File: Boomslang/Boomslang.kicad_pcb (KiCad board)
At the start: 2 copper layers, 100 x 100 mm, 99 parts, among them J1 Screw_Terminal_01x04, J2 Screw_Terminal_01x04, J3 Screw_Terminal_01x04, J4 01x04, J5 Screw_Terminal_01x02, J6 Screw_Terminal_01x02, Q1 IRLZ44N, Q10 2N3904, Q11 IRLZ44N, Q12 2N3904, Q13 2N3904, Q14 2N3904, Q15 2N3906, Q16 2N3904, Q17 IRLZ44N, Q18 2N3904, Q19 2N2222A, Q2 2N3904, Q20 2N2222A, Q3 2N3906, Q4 2N3904, Q5 2N3904, Q6 2N3904, Q7 2N3904, Q8 2N3904, Q9 2N3906, U1 L7805

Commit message: Break out GPIO2 battery sense and GPIO12-14 test points
Adds the GPIO2 12V battery-voltage sense (1:11 divider, matches
firmware's PIN_BATTERY/BATTERY_DIVIDER_RATIO) and breaks out
GPIO12-14 as spare test points for timing tests and similar bring-up
work. Regenerated gerbers and schematic/board renders to match.
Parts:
- added C13: 100 pF, Capacitor_THT:C_Disc_D5.0mm_W2.5mm_P5.00mm, F.Cu at (108.0, 136.7)
- added J7: Conn_01x04_Pin, Connector_PinSocket_2.54mm:PinSocket_1x04_P2.54mm_Vertical, F.Cu at (143.3, 102.6)
- added R45: 100k, Resistor_THT:R_Axial_DIN0207_L6.3mm_D2.5mm_P7.62mm_Horizontal, F.Cu at (127.5, 86.6)
- added R46: 100k, Resistor_THT:R_Axial_DIN0207_L6.3mm_D2.5mm_P7.62mm_Horizontal, F.Cu at (154.4, 51.6)
- added R47: 100k, Resistor_THT:R_Axial_DIN0207_L6.3mm_D2.5mm_P7.62mm_Horizontal, F.Cu at (165.9, 81.8)
- added R48: 100k, Resistor_THT:R_Axial_DIN0207_L6.3mm_D2.5mm_P7.62mm_Horizontal, F.Cu at (168.1, 112.1)
- added R49: 10k, Resistor_THT:R_Axial_DIN0207_L6.3mm_D2.5mm_P7.62mm_Horizontal, F.Cu at (108.0, 134.4)
- added R50: 100k, Resistor_THT:R_Axial_DIN0207_L6.3mm_D2.5mm_P7.62mm_Horizontal, F.Cu at (104.6, 126.7)
- D10, D8, D9: value LED -> WHITE/BLUE LED
- D4, D5, D6, D7: value LED -> RED LED
- R11, R24, R3: value 10k -> 2k2
- moved R34 5.36 mm to (179.6, 113.0)
- moved Q6 5.00 mm to (154.4, 67.1)
- moved R22 3.43 mm to (178.8, 83.3)
- moved D2 1.78 mm to (103.1, 90.4)
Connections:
- DB1 pad 18: unconnected-(DB1-12-Pad18) -> Net-(DB1-12)
- DB1 pad 19: unconnected-(DB1-13-Pad19) -> Net-(DB1-13)
- DB1 pad 20: unconnected-(DB1-14-Pad20) -> Net-(DB1-14)
- DB1 pad 40: unconnected-(DB1-2-Pad40) -> PWRSENSE
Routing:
- net CONTINUITY2: track 15.9 -> 26.4 mm
- net PWRSENSE: track 0.00 -> 10.3 mm
- net CONTINUITY3: track 19.9 -> 28.9 mm
- net Net-(DB1-14): track 0.00 -> 5.59 mm
- net Net-(DB1-13): track 0.00 -> 5.59 mm
- net Net-(DB1-12): track 0.00 -> 5.59 mm
- net Net-(J3-Pin_1): track 24.1 -> 20.5 mm
- net +12V: track 157.0 -> 160.4 mm
- net FAILSAFE: track 156.2 -> 153.5 mm
- net Net-(Q2-B): track 60.6 -> 63.4 mm
- net Net-(Q6-B): track 33.3 -> 35.8 mm
- net SENSEFAILSAFE: track 64.0 -> 66.0 mm
- net FAULT: track 153.8 -> 155.6 mm
- net Net-(J2-Pin_1): track 27.8 -> 26.2 mm
- net SENSE1: track 60.7 -> 61.9 mm
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
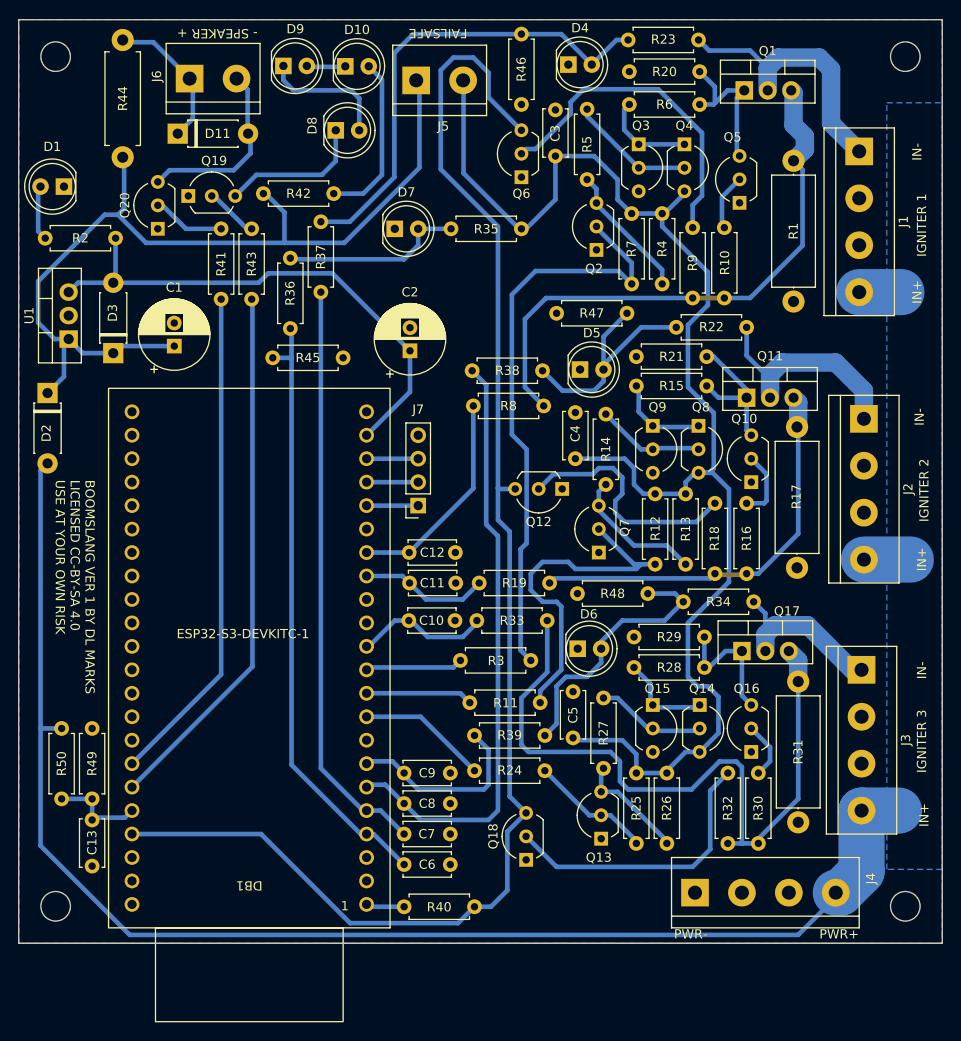
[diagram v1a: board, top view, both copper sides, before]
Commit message: Add snubbers to MOSFET drains
RC snubber on each channel's IRLZ44N drain to damp switching
transients from the igniter/wiring inductance. Regenerated gerbers
and schematic/board renders to match.
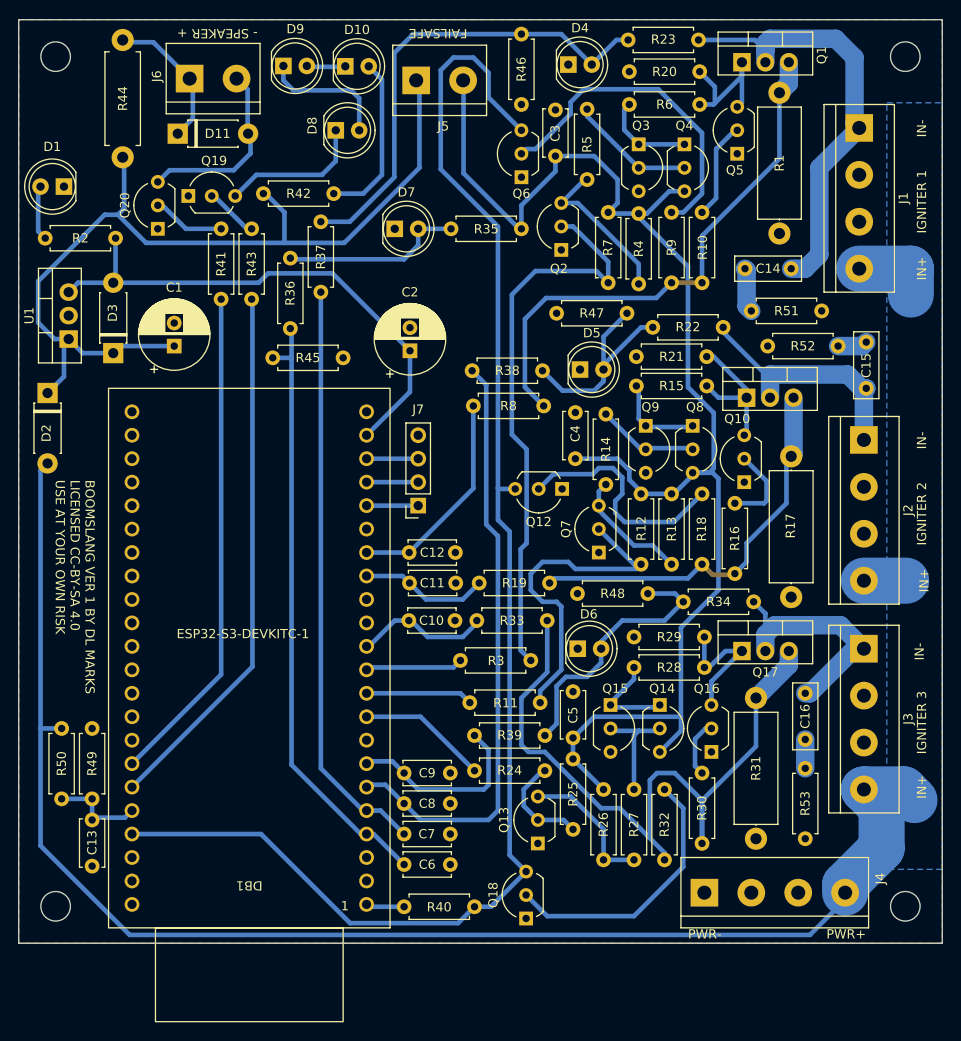
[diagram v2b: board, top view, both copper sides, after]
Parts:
- added C14: 220 nF, Capacitor_THT:C_Rect_L7.0mm_W2.5mm_P5.00mm, F.Cu at (183.6, 77.0)
- added C15: 220 nF, Capacitor_THT:C_Rect_L7.0mm_W2.5mm_P5.00mm, F.Cu at (191.8, 89.9)
- added C16: 220 nF, Capacitor_THT:C_Rect_L7.0mm_W2.5mm_P5.00mm, F.Cu at (185.2, 122.9)
- added R51: 2R2, Resistor_THT:R_Axial_DIN0207_L6.3mm_D2.5mm_P7.62mm_Horizontal, F.Cu at (179.3, 81.5)
- added R52: 2R2, Resistor_THT:R_Axial_DIN0207_L6.3mm_D2.5mm_P7.62mm_Horizontal, F.Cu at (188.7, 85.3)
- added R53: 2R2, Resistor_THT:R_Axial_DIN0207_L6.3mm_D2.5mm_P7.62mm_Horizontal, F.Cu at (185.2, 131.1)
- moved R27 10.4 mm to (166.6, 133.3)
- moved R1 7.52 mm to (182.4, 57.9)
- moved R26 7.08 mm to (163.3, 133.3)
- moved R32 7.08 mm to (169.9, 133.3)
- moved R25 7.03 mm to (160.0, 130.0)
- moved Q13 6.88 mm to (156.2, 139.2)
- moved Q18 6.35 mm to (154.9, 147.3)
- moved R30 6.10 mm to (174.0, 139.2)
- moved Q5 5.32 mm to (177.8, 64.5)
- moved R31 4.91 mm to (179.8, 123.4)
- moved Q15 4.57 mm to (164.1, 124.2)
- moved Q16 4.32 mm to (175.0, 129.3)
- moved Q14 4.32 mm to (169.4, 124.2)
- moved Q2 3.81 mm to (158.8, 74.9)
- moved R17 3.24 mm to (183.6, 97.3)
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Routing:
- net Net-(J1-Pin_1): track 29.2 -> 47.5 mm
- net +12V: track 160.4 -> 170.0 mm
- net Net-(J3-Pin_1): track 20.5 -> 28.1 mm
- net Net-(C14-Pad2): track 0.00 -> 4.85 mm
- net Net-(Q5-B): track 6.12 -> 10.6 mm
- net Net-(C15-Pad2): track 0.00 -> 3.23 mm
- net Net-(C16-Pad2): track 0.00 -> 3.13 mm
- net SENSE1: track 61.9 -> 58.8 mm
- net Net-(Q13-C): track 12.2 -> 15.2 mm
- net Net-(J2-Pin_1): track 26.2 -> 29.0 mm
- net CONTINUITY2: track 26.4 -> 23.9 mm
- net Net-(Q2-C): track 14.7 -> 17.1 mm
- net Net-(Q13-B): track 13.3 -> 11.3 mm
- net Net-(Q18-B): track 31.1 -> 29.4 mm
- net Net-(Q10-B): track 7.52 -> 9.11 mm
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
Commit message: Changed snubber resistor footprint
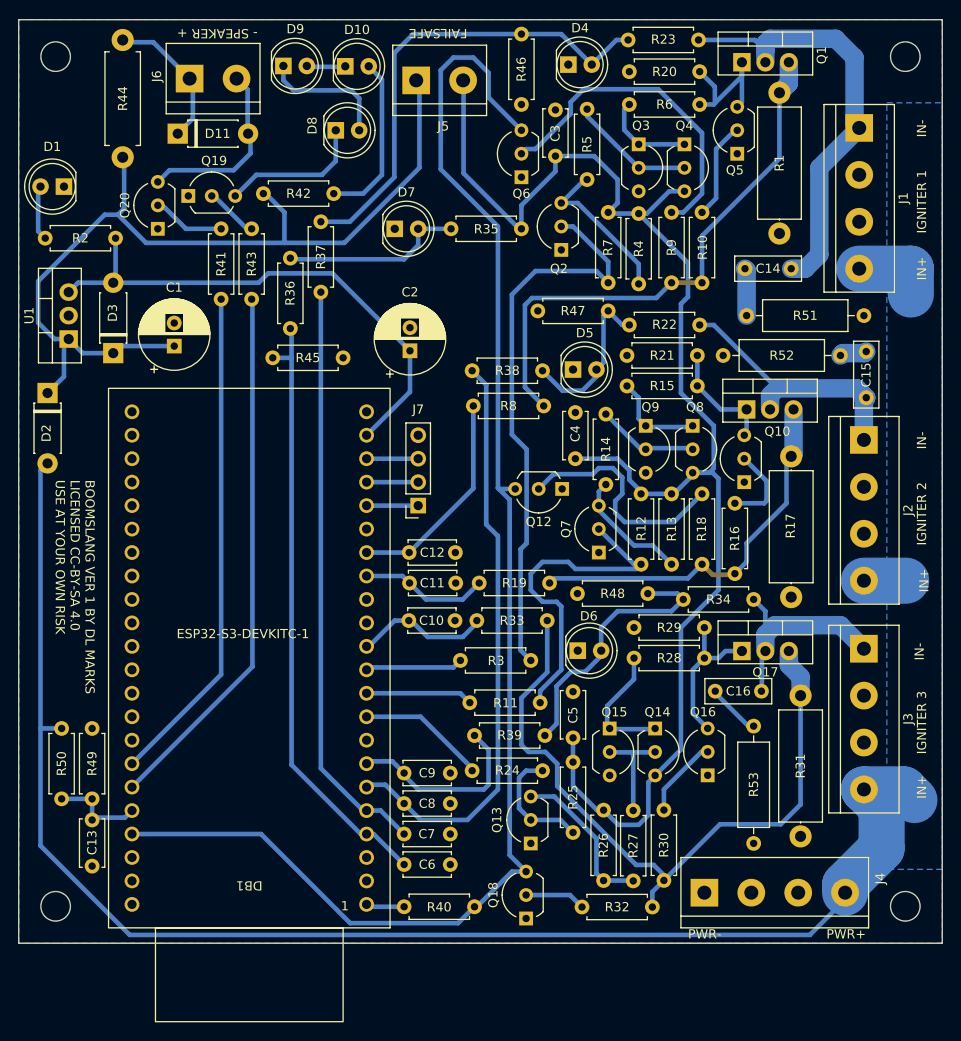
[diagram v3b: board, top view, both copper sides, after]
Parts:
- R51, R52, R53: footprint Resistor_THT:R_Axial_DIN0207_L6.3mm_D2.5mm_P7.62mm_Horizontal -> Resistor_THT:R_Axial_DIN0309_L9.0mm_D3.2mm_P12.70mm_Horizontal
- moved R32 15.6 mm to (161.0, 146.1), turned to 0 degrees
- moved R53 7.22 mm to (179.6, 126.5)
- moved R30 5.76 mm to (169.9, 143.2)
- moved R31 4.83 mm to (184.7, 123.2)
- moved C16 4.75 mm to (180.4, 122.7), turned to 180 degrees
- moved Q14 2.59 mm to (168.9, 126.8)
- moved Q16 2.57 mm to (174.6, 131.8)
- moved R22 2.55 mm to (173.7, 83.1)
- moved Q15 2.55 mm to (164.0, 126.8)
- moved R27 2.28 mm to (166.5, 135.6)
- moved R26 2.24 mm to (163.3, 135.6)
- moved R47 2.05 mm to (163.8, 81.5)
- moved Q11 1.27 mm to (178.8, 92.2)
- moved R52 1.05 mm to (189.0, 86.4)
- moved R21 1.02 mm to (173.5, 86.4)
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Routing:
- net Net-(Q18-B): track 29.4 -> 6.59 mm
- net CONTINUITY2: track 23.9 -> 17.9 mm
- net FAILSAFE: track 153.7 -> 157.7 mm
- net Net-(J3-Pin_1): track 28.1 -> 24.6 mm
- net Net-(Q14-E): track 10.7 -> 13.9 mm
- net Net-(Q10-C): track 15.7 -> 12.6 mm
- net Net-(C16-Pad2): track 3.13 -> 5.84 mm
- net Net-(Q16-B): track 6.25 -> 8.66 mm
- net Net-(Q13-C): track 15.2 -> 17.1 mm
- net Net-(Q13-B): track 11.3 -> 13.1 mm
- net SENSE3: track 78.1 -> 76.6 mm
- net Net-(C8-Pad1): track 65.1 -> 63.8 mm
- net SENSE2: track 43.1 -> 41.8 mm
- net Net-(Q16-C): track 15.3 -> 16.5 mm
- net SENSE1: track 58.8 -> 59.7 mm
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
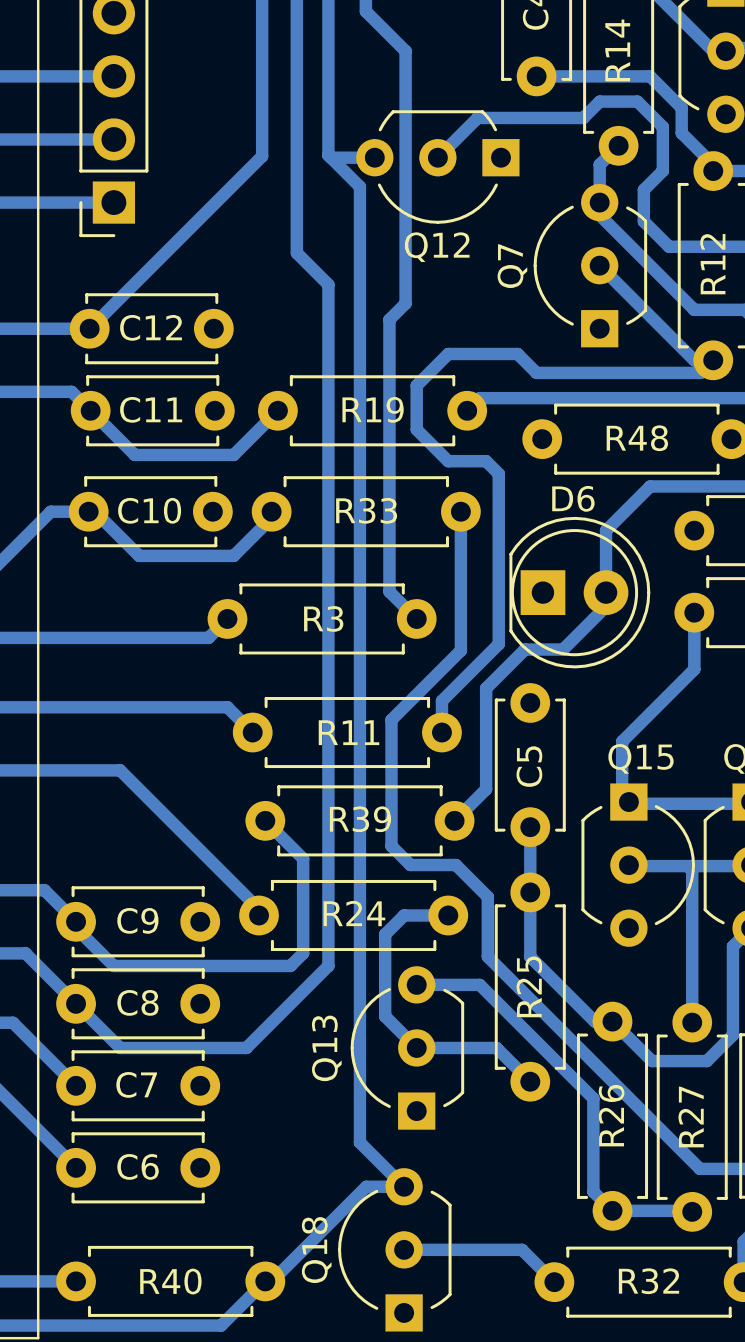
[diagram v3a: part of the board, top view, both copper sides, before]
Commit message: Reduce overcurrent comparator base resistor from 1k to 100R
Bench testing (scoped) found the local per-channel overcurrent
comparator's pull-down transistor base resistor was slowing its own
turn-on, letting fault current overshoot well past the ~13A trip
threshold (38A) before the gate was actually pulled down. Reducing the
base resistor from 1k to 100R speeds up that transistor's reaction,
cutting the overshoot to ~15A. Verified in QUCS-S/ngspice simulation
(Simulations/ThresholdTrip) as well as on the bench.

Adds the QUCS-S simulation used to verify this.
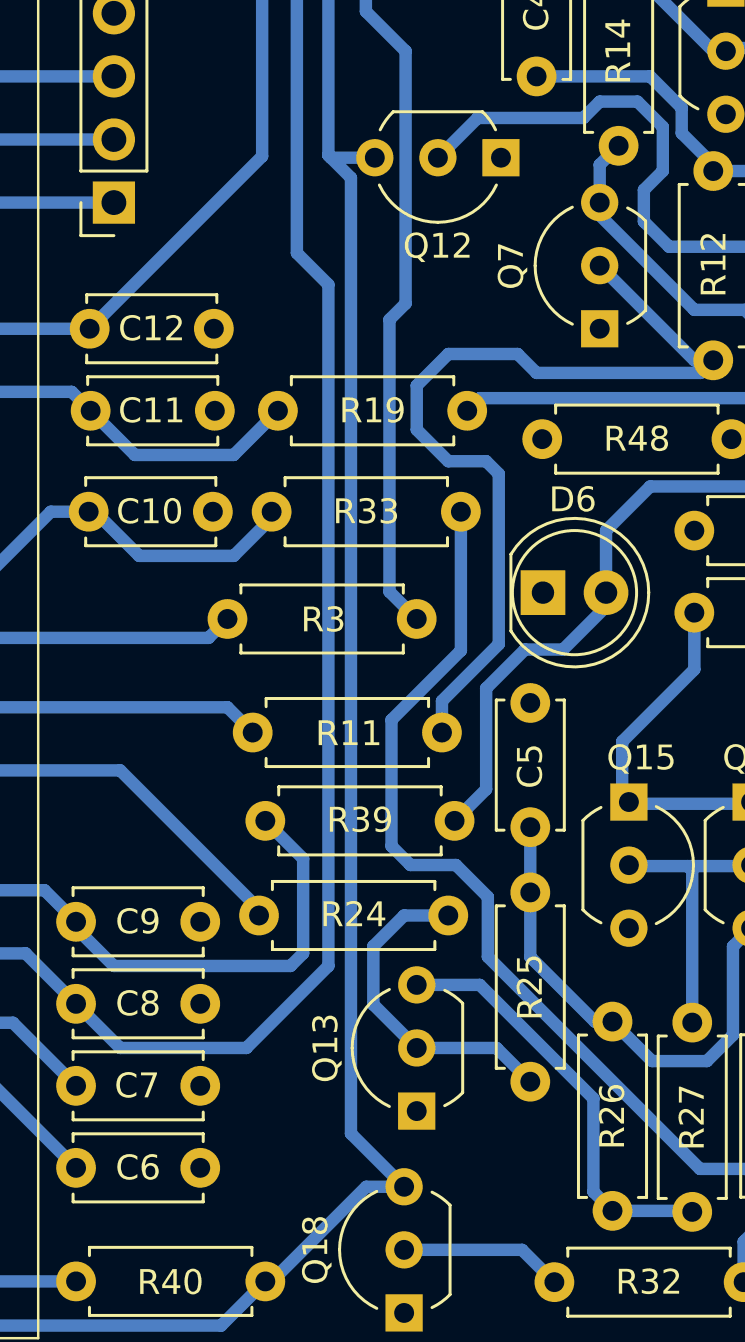
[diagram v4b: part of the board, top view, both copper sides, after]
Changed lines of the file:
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@@
   (segment (start 171.958 70.866) (end 173.99 68.834) (width 0.5) (layer "B.Cu") (net 29))
   (segment (start 153.76 100.81) (end 151.992 100.81) (width 0.5) (layer "B.Cu") (net 30))
-  (segment (start 154.94 142.24) (end 153.162 140.462) (width 0.5) (layer "B.Cu") (net 30))
   (segment (start 154.94 142.24) (end 153.416 142.24) (width 0.5) (layer "B.Cu") (net 30))
   (segment (start 151.892 72.39) (end 145.7 66.198) (width 0.5) (layer "B.Cu") (net 30))
   (segment (start 153.416 142.24) (end 149.606 146.05) (width 0.5) (layer "B.Cu") (net 30))
-  (segment (start 153.162 140.462) (end 153.162 101.98) (width 0.5) (layer "B.Cu") (net 30))
   (segment (start 151.992 100.81) (end 151.892 100.71) (width 0.5) (layer "B.Cu") (net 30))
   (segment (start 145.7 66.198) (end 145.7 55.468) (width 0.5) (layer "B.Cu") (net 30))
@@
   (segment (start 126.238 138.176) (end 135.89 147.828) (width 0.5) (layer "B.Cu") (net 30))
   (segment (start 151.892 100.71) (end 151.892 72.39) (width 0.5) (layer "B.Cu") (net 30))
-  (segment (start 153.162 101.98) (end 151.892 100.71) (width 0.5) (layer "B.Cu") (net 30))
   (segment (start 150.876 55.753) (end 150.876 58.42) (width 0.5) (layer "B.Cu") (net 30))
+  (segment (start 152.8 140.1) (end 152.8 101.618) (width 0.5) (layer "B.Cu") (net 30))
+  (segment (start 152.8 101.618) (end 151.892 100.71) (width 0.5) (layer "B.Cu") (net 30))
   (segment (start 112.268 138.176) (end 126.238 138.176) (width 0.5) (layer "B.Cu") (net 30))
   (segment (start 145.7 55.468) (end 147.066 54.102) (width 0.5) (layer "B.Cu") (net 30))
@@
   (segment (start 147.574 147.828) (end 149.352 146.05) (width 0.5) (layer "B.Cu") (net 30))
   (segment (start 149.606 146.05) (end 149.352 146.05) (width 0.5) (layer "B.Cu") (net 30))
+  (segment (start 154.94 142.24) (end 152.8 140.1) (width 0.5) (layer "B.Cu") (net 30))
   (segment (start 135.89 147.828) (end 147.574 147.828) (width 0.5) (layer "B.Cu") (net 30))
   (segment (start 147.066 54.102) (end 149.225 54.102) (width 0.5) (layer "B.Cu") (net 30))
@@
   (segment (start 180.42 122.71) (end 180.47 122.66) (width 0.5) (layer "B.Cu") (net 49))
   (segment (start 188.976 115.57) (end 181.864 115.57) (width 2) (layer "B.Cu") (net 49))
-  (segment (start 155.448 136.652) (end 154.178 135.382) (width 0.5) (layer "B.Cu") (net 52))
-  (segment (start 154.178 132.08) (end 154.94 131.318) (width 0.5) (layer "B.Cu") (net 52))
+  (segment (start 153.7 132.558) (end 154.94 131.318) (width 0.5) (layer "B.Cu") (net 52))
   (segment (start 155.448 136.652) (end 158.662 136.652) (width 0.5) (layer "B.Cu") (net 52))
   (segment (start 154.94 131.318) (end 156.718 131.318) (width 0.5) (layer "B.Cu") (net 52))
   (segment (start 158.662 136.652) (end 160.02 138.01) (width 0.5) (layer "B.Cu") (net 52))
-  (segment (start 154.178 135.382) (end 154.178 132.08) (width 0.5) (layer "B.Cu") (net 52))
+  (segment (start 153.7 134.904) (end 153.7 132.558) (width 0.5) (layer "B.Cu") (net 52))
+  (segment (start 155.448 136.652) (end 153.7 134.904) (width 0.5) (layer "B.Cu") (net 52))
   (segment (start 162.56 138.684) (end 157.988 134.112) (width 0.5) (layer "B.Cu") (net 53))
   (segment (start 162.56 142.44) (end 162.56 138.684) (width 0.5) (layer "B.Cu") (net 53))
